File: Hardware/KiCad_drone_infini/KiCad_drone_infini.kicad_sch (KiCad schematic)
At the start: 3 parts, among them U1 STM32H743VITx, U2 INA226, U3 LSM6DS3

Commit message: PCB schematic update
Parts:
- added C1, C3, C5: 100nF, symbol Device:C_Small
- added C2: 10uF, symbol Device:C_Small
- added C4: 1uF, symbol Device:C_Small
- added IC1: TESEO-LIV3R, TESEOLIV3R, symbol TESEO-LIV3R:TESEO-LIV3R
- added IC2: LD1117D33TR, SOIC127P600X175-8N, symbol LD1117D33TR:LD1117D33TR
- added IC3: L4973D5.1-013TR, SOIC127P1032X265-20N, symbol L4973D5_1-013TR:L4973D5.1-013TR
- added J1, J2, J3, J4: Conn_01x03, symbol Connector_Generic:Conn_01x03
- added R1, R2, R3, R4, R5, R6: R_Small, symbol Device:R_Small
- added U4: MPL3115A2, Package_LGA:NXP_LGA-8_3x5mm_P1.25mm_H1.1mm, symbol Sensor_Pressure:MPL3115A2
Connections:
- net GND: now reaches U3.2 (SDX)
- net GND: now also U2.7 (GND), U2.9 (Vin-), U3.3 (SCX), U3.6 (GND), U3.7 (GND), C1.2, C2.2, C3.2, C4.2, C5.1, R5.2, R6.1, U4.3 (GND)
- net VDDIO: now reaches U3.5 (VDDIO)
- net VDDIO: now also R6.2
- net 3.3V: now reaches U3.8 (VDD)
- net 3.3V: now also C2.1, C3.1, C5.2, U4.1 (VDD)
- net Load: now reaches U2.10 (Vin+)
- net Load: now also R4.2, R5.1
- net at U2.3 (~{Alert}): now also R3.2
- net at U2.4 (SDA): now also R1.2
- net at U2.5 (SCL): now also R2.2
- net Supply Voltage: now reaches U2.6 (VS)
- net Supply Voltage: now also C4.1, R1.1, R2.1, R3.1
- net Bus Voltage: now reaches U2.8 (Vbus)
- net Bus Voltage: now also R4.1
- new net: C1.1, U4.2 (CAP)
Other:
- note added: "Baromètre MPL3115A2ST1"
- note added: "Buck L4973D5.1-013TR"
- note added: "Connecteur Camera"
- note added: "Connecteur_ESC"
- note added: "Connecteur_Servos"
- note added: "GPS TESEO-LIV3R"
- note added: "LDO LD1117D33TR à changer"
- moved on the sheet: U1, U2, U3

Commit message: update KiCad
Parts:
- removed IC2: LD1117D33TR, SOIC127P600X175-8N, symbol LD1117D33TR:LD1117D33TR
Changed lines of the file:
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@@
-	)
-	(symbol
-		(lib_id "LD1117D33TR:LD1117D33TR")
-		(at 175.26 143.51 0)
-		(unit 1)
-		(exclude_from_sim no)
-		(in_bom yes)
-		(on_board yes)
-		(dnp no)
-		(fields_autoplaced yes)
-		(property "Reference" "IC2"
-			(at 193.04 135.89 0)
-			(effects
-				(font
-					(size 1.27 1.27)
-				)
-			)
-		)
-		(property "Value" "LD1117D33TR"
-			(at 193.04 138.43 0)
-			(effects
-				(font
-					(size 1.27 1.27)
-				)
-			)
-		)
-		(property "Footprint" "SOIC127P600X175-8N"
-			(at 207.01 238.43 0)
-			(effects
-				(font
-					(size 1.27 1.27)
-				)
-				(justify left top)
-				(hide yes)
-			)
-		)
-		(property "Datasheet" "http://www.st.com/st-web-ui/static/active/en/resource/technical/document/datasheet/CD00000544.pdf"
-			(at 207.01 338.43 0)
-			(effects
-				(font
-					(size 1.27 1.27)
-				)
-				(justify left top)
-				(hide yes)
-			)
-		)
-		(property "Description" "LD1117D33TR, Low Dropout Voltage Regulator, 1.3A, 3.3V +/-1%, 8-Pin SO"
-			(at 175.26 143.51 0)
-			(effects
-				(font
-					(size 1.27 1.27)
-				)
-				(hide yes)
-			)
-		)
-		(property "Height" "1.75"
-			(at 207.01 538.43 0)
-			(effects
-				(font
-					(size 1.27 1.27)
-				)
-				(justify left top)
-				(hide yes)
-			)
-		)
-		(property "Mouser Part Number" "511-LD1117D33-TR"
-			(at 207.01 638.43 0)
-			(effects
-				(font
-					(size 1.27 1.27)
-				)
-				(justify left top)
-				(hide yes)
-			)
-		)
-		(property "Mouser Price/Stock" "https://www.mouser.co.uk/ProductDetail/STMicroelectronics/LD1117D33TR?qs=8YYpzd7qSxIl%2FiC6F%2FA2nA%3D%3D"
-			(at 207.01 738.43 0)
-			(effects
-				(font
-					(size 1.27 1.27)
-				)
-				(justify left top)
-				(hide yes)
-			)
-		)
-		(property "Manufacturer_Name" "STMicroelectronics"
-			(at 207.01 838.43 0)
-			(effects
-				(font
-					(size 1.27 1.27)
-				)
-				(justify left top)
-				(hide yes)
-			)
-		)
-		(property "Manufacturer_Part_Number" "LD1117D33TR"
-			(at 207.01 938.43 0)
-			(effects
-				(font
-					(size 1.27 1.27)
-				)
-				(justify left top)
-				(hide yes)
-			)
-		)
-		(pin "2"
-		)
-		(pin "6"
-		)
-		(pin "3"
-		)
-		(pin "1"
-		)
-		(pin "4"
-		)
-		(pin "8"
-		)
-		(pin "5"
-		)
-		(pin "7"
-		)
-		(instances
-			(project ""
-				(path "/ec544f58-99e1-4130-8ccd-230881991a80"
-					(reference "IC2")
-					(unit 1)
-				)
-			)
-		)
 	)
 	(symbol

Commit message: Modif Kicad 28/11
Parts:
- added C0: 100u, symbol Device:C_Small
- added C6: 100nF, symbol Device:C_Small
- added C7: 20u, symbol Device:C_Small
- added C8: 220n, symbol Device:C_Small
- added C9: 22u, symbol Device:C_Small
- added Cosc: ?, symbol Device:C_Small
- added D1: D_Small, symbol Device:D_Small
- added J5: Conn_ST_STDC14, Connector_PinHeader_1.27mm:PinHeader_2x07_P1.27mm_Vertical_SMD, symbol Connector:Conn_ST_STDC14
- added L1: 150u, symbol Device:L_Small
- added PS1: 173020536, 173020536, symbol buck_173020536:173020536
- added R7: 10k, symbol Device:R_Small
- added Rosc: ?, symbol Device:R_Small
- R6: value R_Small -> 10k
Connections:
- net 3.3V: now also IC1.6 (VBATT), IC1.7 (VCC_IO), IC1.8 (VCC), R6.1, U3.12 (CS), U3.5 (VDDIO), C6.2, R7.1
- net GND: now also IC1.1 (GND), IC1.10 (_GND_RF), IC1.12 (GND_RF), IC3.14 (GND_5), IC3.15 (GND_6), IC3.16 (GND_7), IC3.17 (GND_8), IC3.4 (GND_1), IC3.5 (GND_2), IC3.6 (GND_3), IC3.7 (GND_4), U3.1 (SDO/SA0), C0.2, C6.1, C7.1, C9.2, Cosc.2, D1.2 (A), J5.11 (GNDDetect), J5.5 (GND), J5.7 (GND), PS1.2 (GND); no longer R6.1
- net SCL_IMU: now reaches U3.13 (SCL)
- net SCL_IMU: now also R7.2
- net SDA_IMU: now reaches U3.14 (SDA)
- net SDA_IMU: now also R6.2
- net Interupt_IMU: now reaches U3.4 (INT1)
- net Control_antenne: now reaches IC1.13 (_ANT_OFF)
- net SDA_GPS: now reaches IC1.16 (SDA)
- net SCL_GPS: now reaches IC1.17 (SCL)
- net Interrupt_GPS: now reaches IC1.5 (_WAKE-UP)
- net OSC: now reaches IC3.1 (OSC)
- net OSC: now also Cosc.1, Rosc.2
- net at IC3.10 (BOOT): now also C8.2
- net at IC3.2 (OUT_1): now also IC3.3 (OUT_2), C8.1, D1.1 (K), L1.2
- net 11.1V: now reaches IC3.8 (VCC_1)
- net 11.1V: now also IC3.9 (VCC_2), C7.2, PS1.1 (VIN), Rosc.1
- removed net VDDIO: R6.2, U3.5 (VDDIO)
- new net 5.1V: C0.1, C9.1, L1.1, PS1.3 (VOUT)
- no-connect marks 0 -> 10
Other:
- note added: "GPS TESEO-LIV3R à voir des capa de decouplages"
- note added: "IMU LSM6DSRXTR"
- note added: "STLink"
- note added: "buck 173020536 Fini"
- note added: "pour alimenter antenne active"
- note removed: "GPS TESEO-LIV3R"
- note removed: "IMU LSM6DSRXTR (pas sûr)"
- moved on the sheet: C1, C2, C3, C5, IC1, IC3, U3, U4

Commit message: Modif KiCad 04/12
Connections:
- net SCL_GPS is gone; now on net I2C1_SCL: IC1.17 (SCL)
- net SCL_IMU is gone; now on net I2C1_SCL: R7.2, U3.13 (SCL)
- net SDA_IMU is gone; now on net I2C1_SDA: R6.2, U3.14 (SDA)
- net GND: no longer U3.2 (SDX), U3.3 (SCX)
- net I2C1_SDA: now reaches U4.7 (SDL)
- net I2C1_SDA: now also U1.93 (PB7)
- net I2C1_SCL: now reaches U4.8 (SCL)
- net I2C1_SCL: now also U1.92 (PB6)
- net GPS_UART_RX_MCU: now reaches IC1.2 (TX)
- net GPS_UART_RX_MCU: now also U1.54 (PB15)
- net GPS_UART_TX_MCU: now reaches IC1.3 (RX)
- net GPS_UART_TX_MCU: now also U1.53 (PB14)
- net STLINK_UART_RX_MCU: now reaches J5.13 (VCP_RX)
- net STLINK_UART_RX_MCU: now also U1.56 (PD9)
- net STLINK_UART_TX_MCU: now reaches J5.14 (VCP_TX)
- net STLINK_UART_TX_MCU: now also U1.55 (PD8)
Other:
- moved on the sheet: C0, C8, Cosc, D1, IC3, L1, Rosc, U1

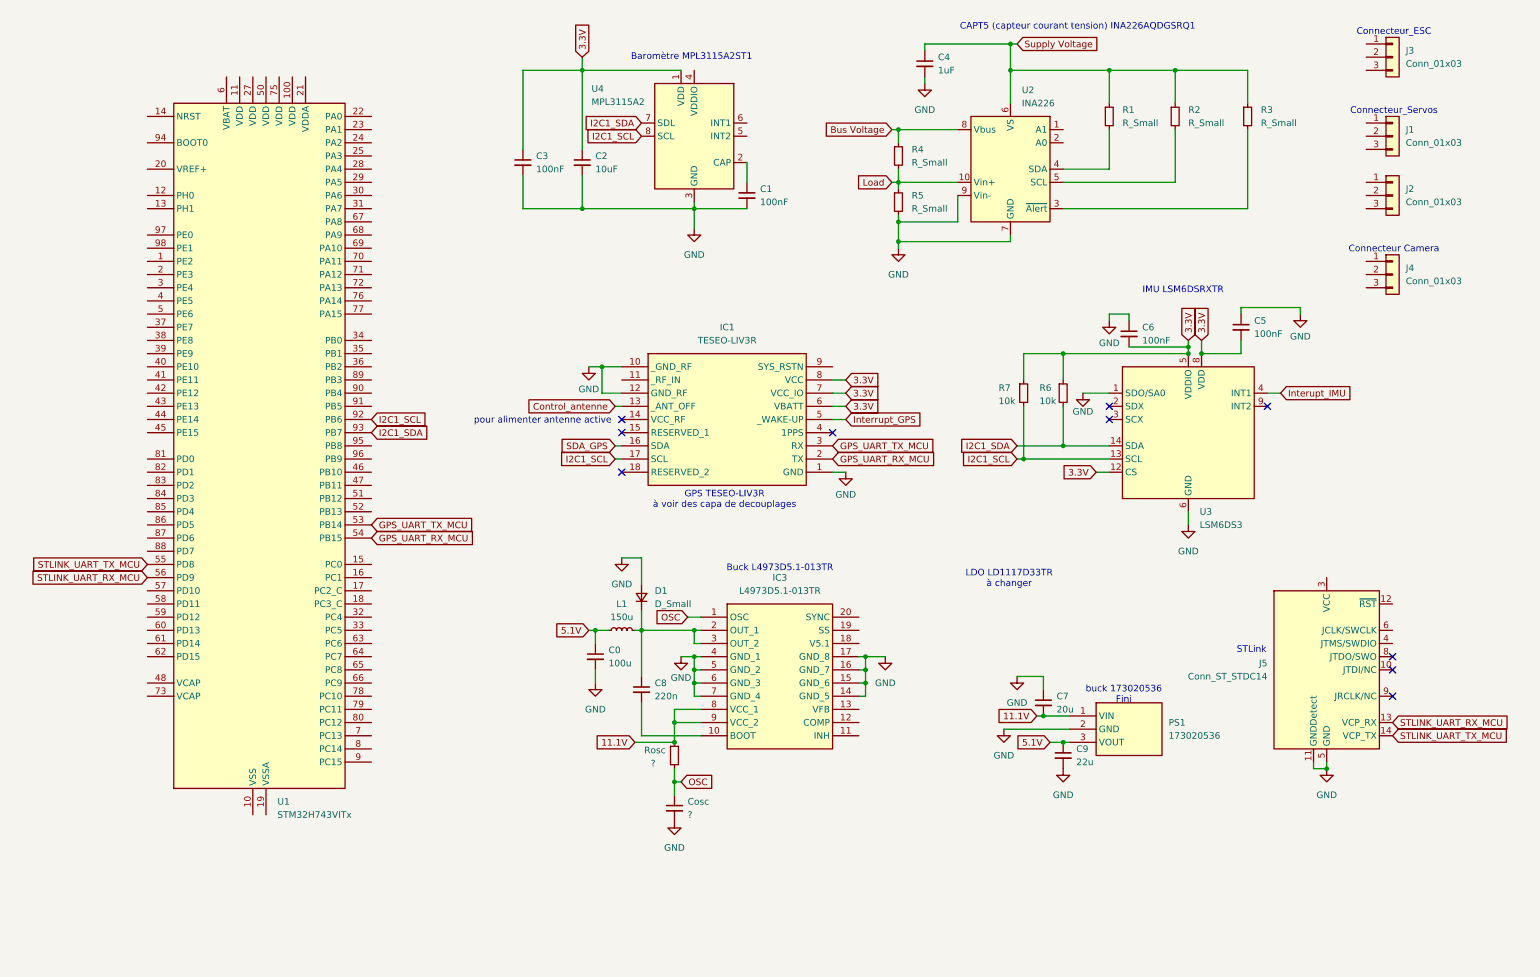
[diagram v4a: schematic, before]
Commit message: PCB schematic update 05/12
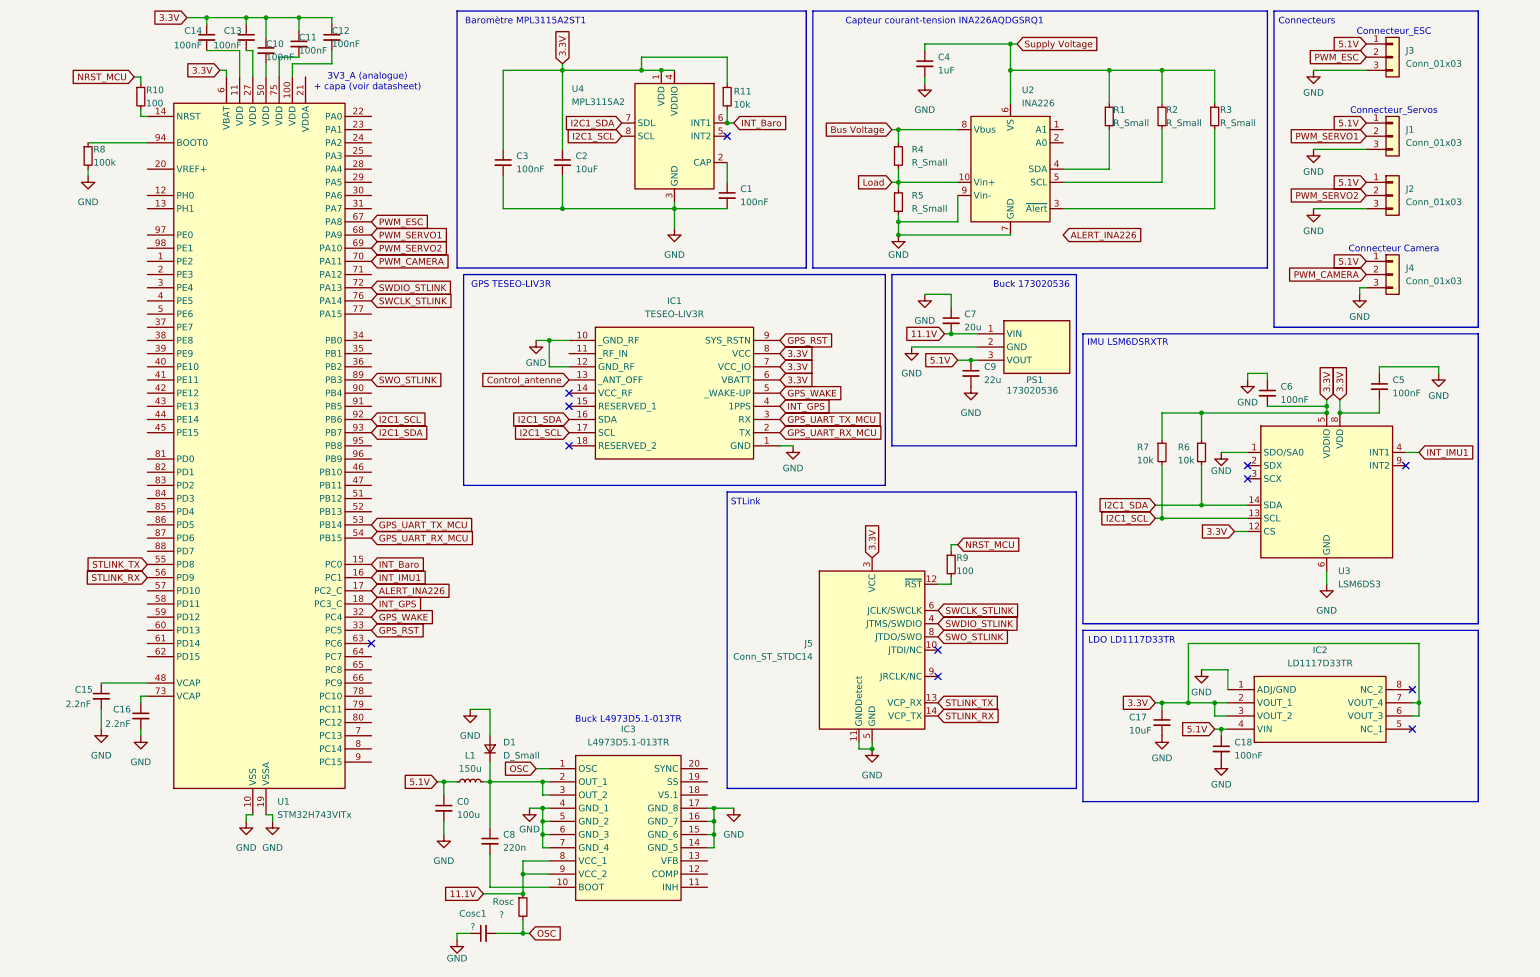
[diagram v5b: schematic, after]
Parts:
- removed Cosc: ?, symbol Device:C_Small
- added C10, C11, C12, C13, C14, C18: 100nF, symbol Device:C_Small
- added C15, C16: 2.2nF, symbol Device:C_Small
- added C17: 10uF, symbol Device:C_Small
- added Cosc1: ?, symbol Device:C_Small
- added IC2: LD1117D33TR, SOIC127P600X175-8N, symbol LD1117D33TR:LD1117D33TR
- added R10, R9: 100, symbol Device:R_Small
- added R11: 10k, symbol Device:R_Small
- added R8: 100k, symbol Device:R_Small
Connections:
- net Interrupt_GPS is gone; now on net GPS_WAKE: IC1.5 (_WAKE-UP)
- net Interupt_IMU is gone; now on net INT_IMU1: U3.4 (INT1)
- net SDA_GPS is gone; now on net I2C1_SDA: IC1.16 (SDA)
- net 3.3V: now also J5.3 (VCC), U1.6 (VBAT), U4.4 (VDDIO), C10.1, C11.1, C12.1, C13.1, C14.1, C17.1, IC2.2 (VOUT_1), IC2.3 (VOUT_2), IC2.6 (VOUT_3), IC2.7 (VOUT_4), R11.1
- net 5.1V: now also J1.1 (Pin_1), J2.1 (Pin_1), J3.1 (Pin_1), J4.1 (Pin_1), C18.1, IC2.4 (VIN)
- net GND: now also J1.3 (Pin_3), J2.3 (Pin_3), J3.3 (Pin_3), J4.3 (Pin_3), U1.10 (VSS), U1.19 (VSSA), U1.26 (VSS), U1.49 (VSS), U1.74 (VSS), U1.99 (VSS), C15.2, C16.2, C17.2, C18.2, Cosc1.1, IC2.1 (ADJ/GND), R8.2
- net OSC: now also Cosc1.2
- net INT_Baro: now reaches U4.6 (INT1)
- net INT_Baro: now also U1.15 (PC0), R11.2
- net INT_GPS: now reaches IC1.4 (1PPS)
- net INT_GPS: now also U1.18 (PC3_C)
- net GPS_RST: now reaches IC1.9 (SYS_RSTN)
- net GPS_RST: now also U1.33 (PC5)
- net PWM_SERVO2: now reaches J2.2 (Pin_2)
- net PWM_SERVO2: now also U1.69 (PA10)
- net PWM_ESC: now reaches J3.2 (Pin_2)
- net PWM_ESC: now also U1.67 (PA8)
- net at J5.12 (~{RST}): now also R9.2
- net SWDIO_STLINK: now reaches J5.4 (JTMS/SWDIO)
- net SWDIO_STLINK: now also U1.72 (PA13)
- net SWCLK_STLINK: now reaches J5.6 (JCLK/SWCLK)
- net SWCLK_STLINK: now also U1.76 (PA14)
- net SWO_STLINK: now reaches J5.8 (JTDO/SWO)
- net SWO_STLINK: now also U1.89 (PB3)
- net PWM_SERVO1: now reaches J1.2 (Pin_2)
- net PWM_SERVO1: now also U1.68 (PA9)
- net PWM_CAMERA: now reaches J4.2 (Pin_2)
- net PWM_CAMERA: now also U1.70 (PA11)
- net at U1.100 (VDD): now also C12.2
- net at U1.11 (VDD): now also C14.2
- net at U1.14 (NRST): now also R10.2
- net INT_IMU1: now reaches U1.16 (PC1)
- net ALERT_INA226: now reaches U1.17 (PC2_C)
- net at U1.27 (VDD): now also C13.2
- net GPS_WAKE: now reaches U1.32 (PC4)
- net at U1.48 (VCAP): now also C15.1
- net at U1.50 (VDD): now also C10.2
- net at U1.73 (VCAP): now also C16.1
- net at U1.75 (VDD): now also C11.2
- net at U1.94 (BOOT0): now also R8.1
- net STLINK_UART_RX_MCU renamed STLINK_RX
- net STLINK_RX: now also J5.14 (VCP_TX); no longer J5.13 (VCP_RX)
- net STLINK_UART_TX_MCU renamed STLINK_TX
- net STLINK_TX: now also J5.13 (VCP_RX); no longer J5.14 (VCP_TX)
- new net NRST_MCU: R10.1, R9.1
- no-connect marks 10 -> 12
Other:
- note added: "3V3_A (analogue) + capa (voir datasheet)"
- note added: "Buck 173020536"
- note added: "Capteur courant-tension INA226AQDGSRQ1"
- note added: "Connecteurs"
- note added: "GPS TESEO-LIV3R"
- note added: "LDO LD1117D33TR"
- note removed: "CAPT5 (capteur courant tension) INA226AQDGSRQ1"
- note removed: "GPS TESEO-LIV3R à voir des capa de decouplages"
- note removed: "LDO LD1117D33TR à changer"
- note removed: "buck 173020536 Fini"
- note removed: "pour alimenter antenne active"
- moved on the sheet: C0, C1, C2, C3, C5, C6, C7, C8, C9, D1, IC1, IC3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
